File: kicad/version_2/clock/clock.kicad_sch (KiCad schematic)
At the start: 34 parts

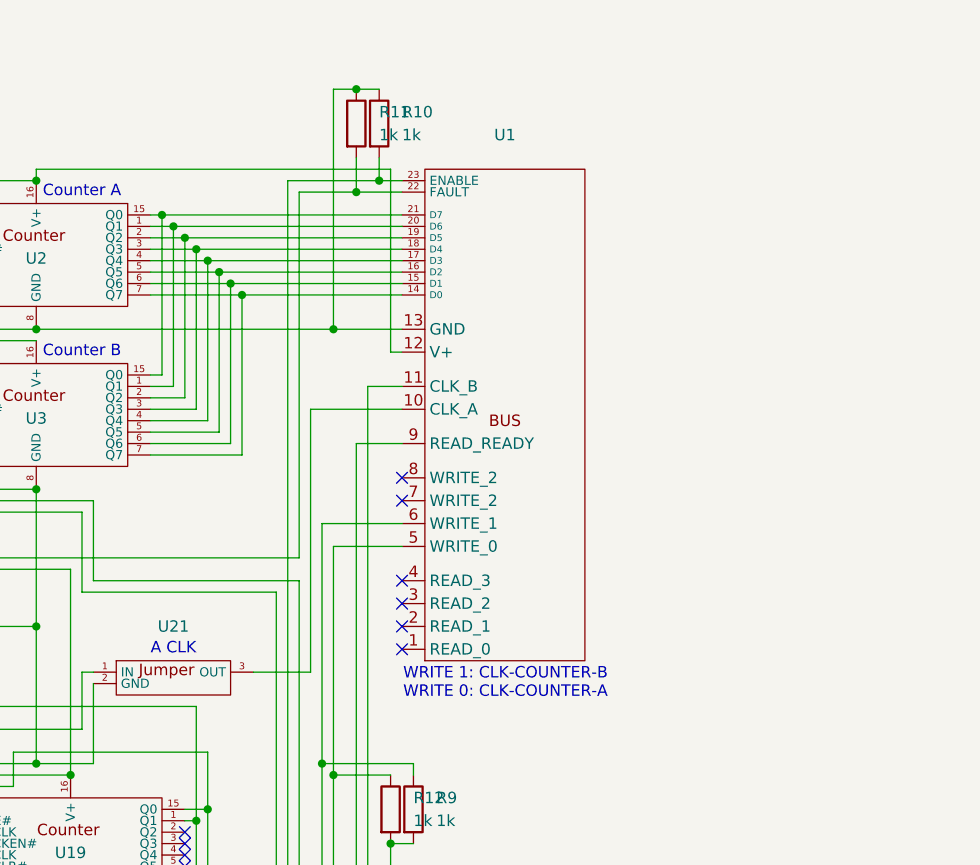
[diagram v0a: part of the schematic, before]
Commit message: Fixed clock board
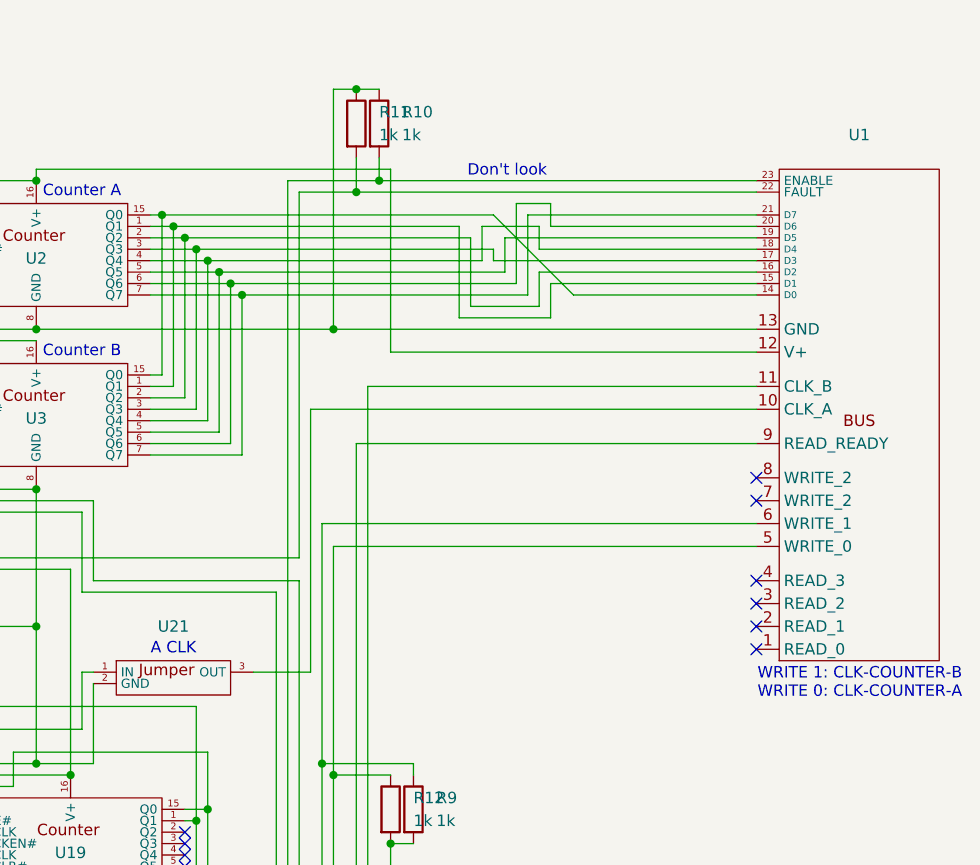
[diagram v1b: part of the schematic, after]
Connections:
- net at U2.7 (Q7), U3.7 (Q7): now also U1.21 (D7); no longer U1.14 (D0)
- net at U2.6 (Q6), U3.6 (Q6): now also U1.20 (D6); no longer U1.15 (D1)
- net at U2.5 (Q5), U3.5 (Q5): now also U1.19 (D5); no longer U1.16 (D2)
- net at U2.4 (Q4), U3.4 (Q4): now also U1.18 (D4); no longer U1.17 (D3)
- net at U2.3 (Q3), U3.3 (Q3): now also U1.17 (D3); no longer U1.18 (D4)
- net at U2.2 (Q2), U3.2 (Q2): now also U1.16 (D2); no longer U1.19 (D5)
- net at U2.1 (Q1), U3.1 (Q1): now also U1.15 (D1); no longer U1.20 (D6)
- net at U2.15 (Q0), U3.15 (Q0): now also U1.14 (D0); no longer U1.21 (D7)
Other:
- note added: "Don't look"
- moved on the sheet: U1
